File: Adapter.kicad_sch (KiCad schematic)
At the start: 0 parts

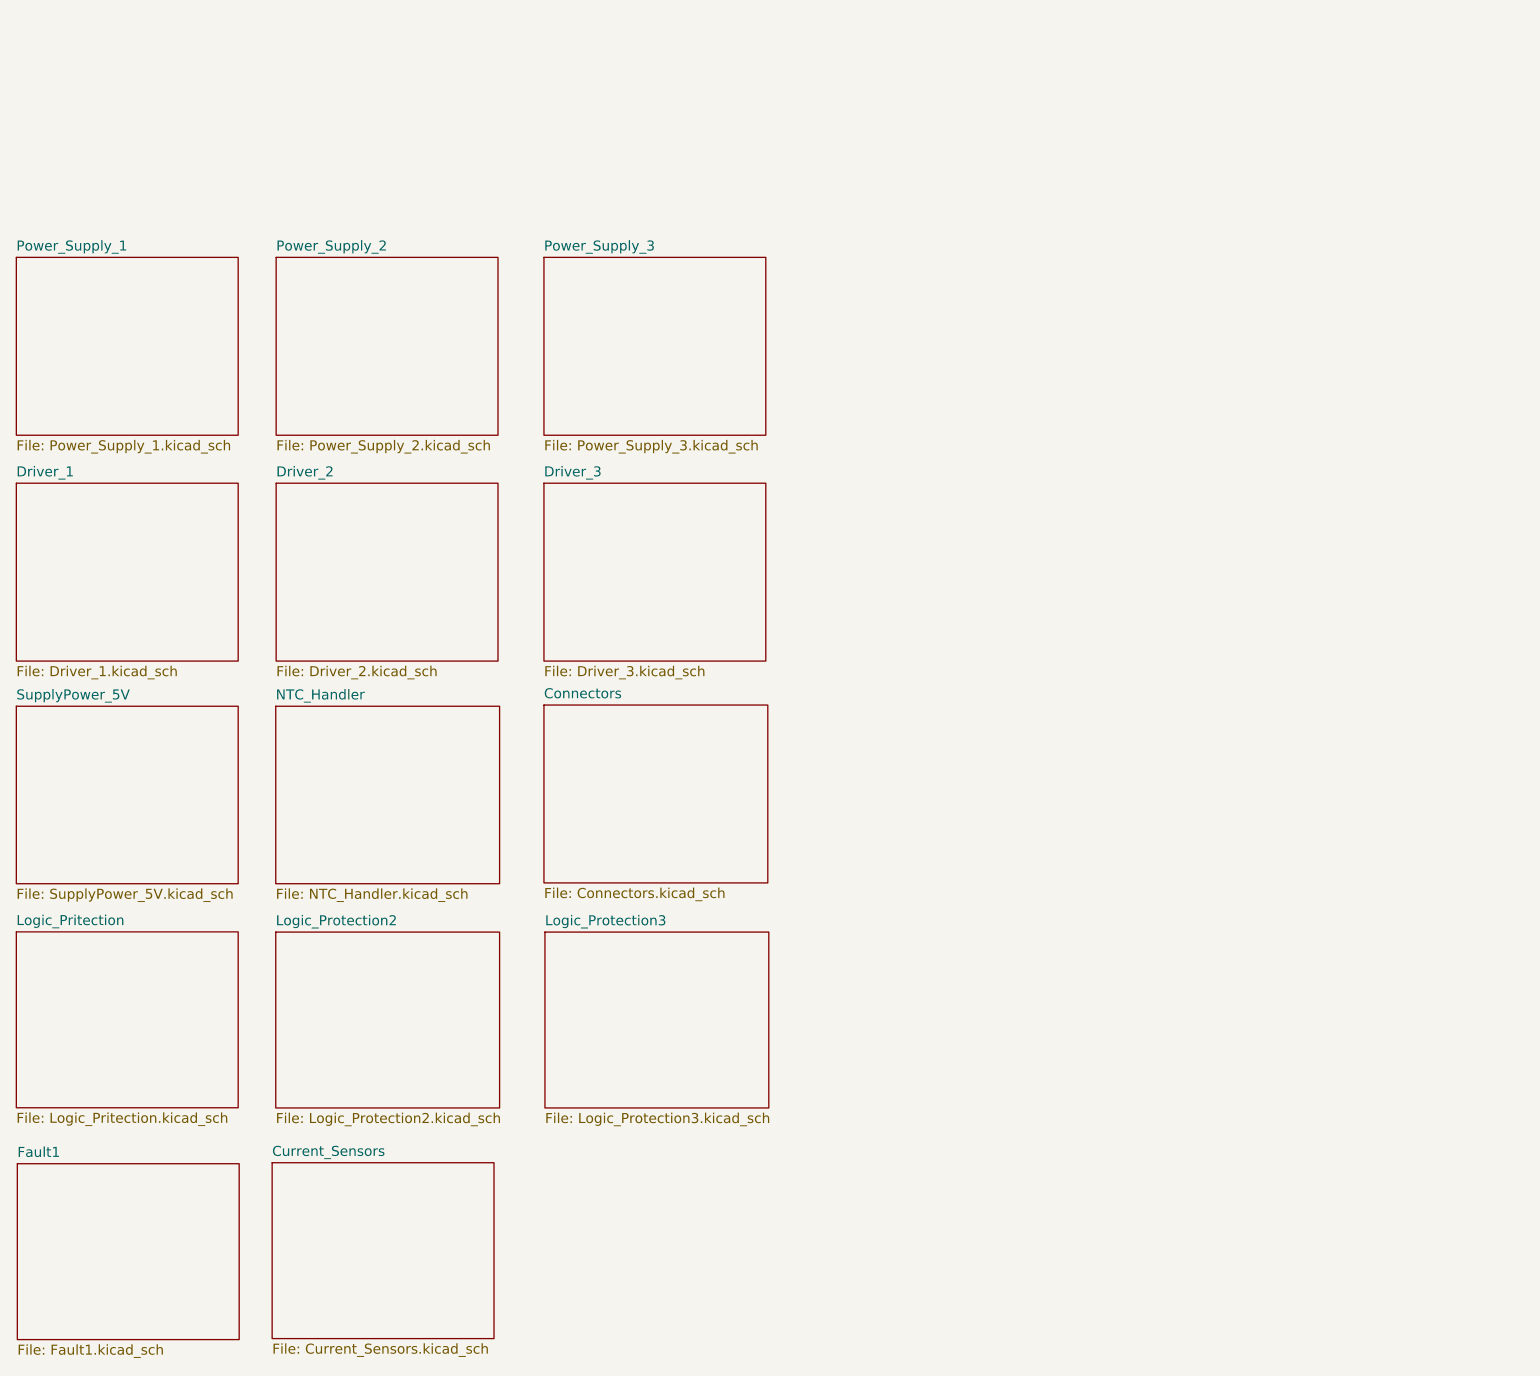
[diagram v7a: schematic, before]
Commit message: VER2.2: добавил фильтры на вход ШИМа и обновил все доки
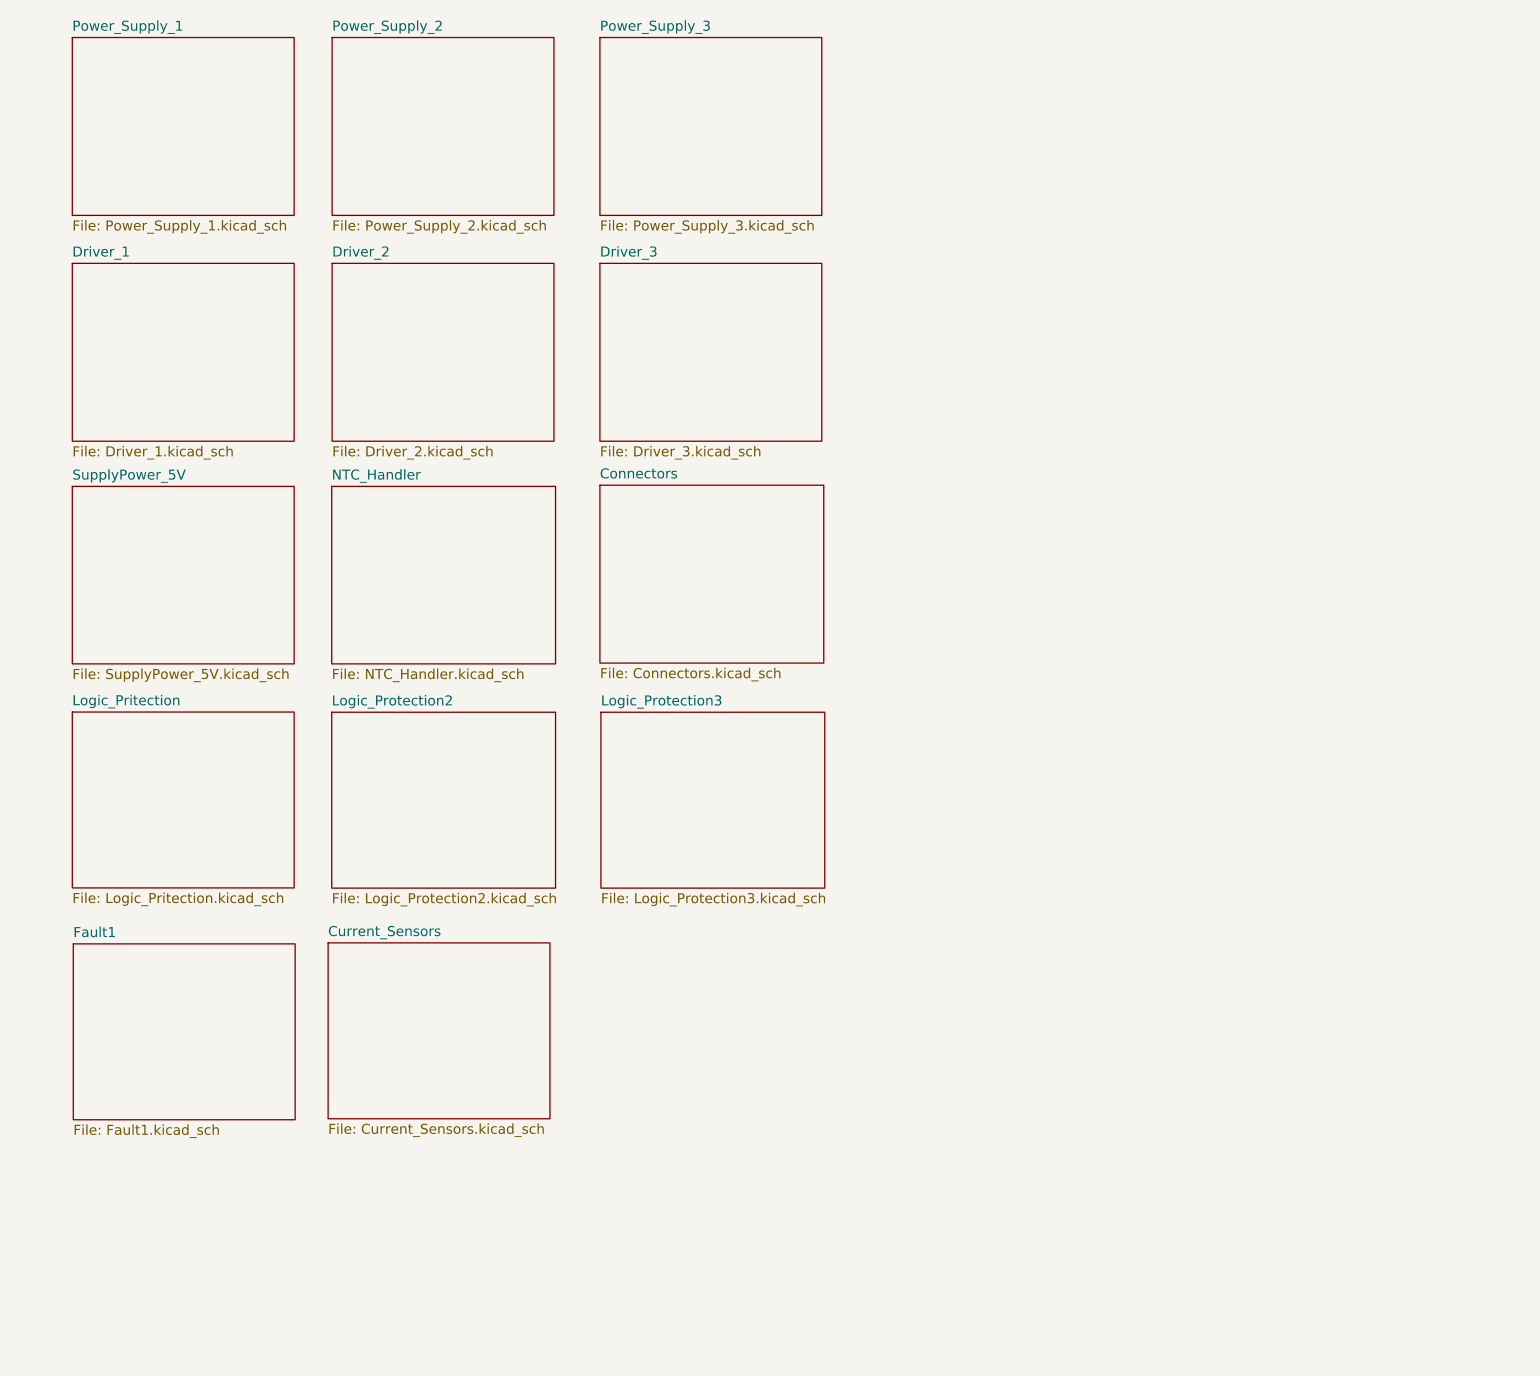
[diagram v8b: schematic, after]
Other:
- company: (none) -> ООО "ЭТТ"
- title: (none) -> Трехфазные драйвера
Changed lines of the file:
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@@
 	(generator "eeschema")
 	(generator_version "9.0")
-	(paper "A4")
-	(sheet
-		(at 18.288 81.28)
+	(paper "A3")
+	(title_block
+		(title "Трехфазные драйвера")
+		(date "2025-06-04")
+		(company "ООО \"ЭТТ\"")
+		(comment 2 "Филатов А.С.")
+		(comment 3 "Сизякин А.В.")
+	)
+	(sheet
+		(at 25.4 53.34)
 		(size 28.194 22.606)
 		(exclude_from_sim no)
@@
 		)
 		(property "Sheetname" "Driver_1"
-			(at 18.288 80.5684 0)
+			(at 25.4 52.6284 0)
 			(effects
 				(font
@@
 		)
 		(property "Sheetfile" "Driver_1.kicad_sch"
-			(at 18.288 104.4706 0)
+			(at 25.4 76.5306 0)
 			(effects
 				(font
@@
 	)
 	(sheet
-		(at 85.344 52.578)
+		(at 92.456 24.638)
 		(size 28.194 22.606)
 		(exclude_from_sim no)
@@
 		)
 		(property "Sheetname" "Power_Supply_3"
-			(at 85.344 51.8664 0)
+			(at 92.456 23.9264 0)
 			(effects
 				(font
@@
 		)
 		(property "Sheetfile" "Power_Supply_3.kicad_sch"
-			(at 85.344 75.7686 0)
+			(at 92.456 47.8286 0)
 			(effects
 				(font
@@
 	)
 	(sheet
-		(at 18.288 109.6264)
+		(at 25.4 81.6864)
 		(size 28.194 22.5552)
 		(exclude_from_sim no)
@@
 		)
 		(property "Sheetname" "SupplyPower_5V"
-			(at 18.288 108.9148 0)
+			(at 25.4 80.9748 0)
 			(effects
 				(font
@@
 		)
 		(property "Sheetfile" "SupplyPower_5V.kicad_sch"
-			(at 18.288 132.7662 0)
+			(at 25.4 104.8262 0)
 			(effects
 				(font
@@
 	)
 	(sheet
-		(at 85.344 81.28)
+		(at 92.456 53.34)
 		(size 28.194 22.606)
 		(exclude_from_sim no)
@@
 		)
 		(property "Sheetname" "Driver_3"
-			(at 85.344 80.5684 0)
+			(at 92.456 52.6284 0)
 			(effects
 				(font
@@
 		)
 		(property "Sheetfile" "Driver_3.kicad_sch"
-			(at 85.344 104.4706 0)
+			(at 92.456 76.5306 0)
 			(effects
 				(font
@@
 	)
 	(sheet
-		(at 50.8 167.64)
+		(at 57.912 139.7)
 		(size 28.194 22.352)
 		(exclude_from_sim no)
@@
 		)
 		(property "Sheetname" "Current_Sensors"
-			(at 50.8 166.9284 0)
+			(at 57.912 138.9884 0)
 			(effects
 				(font
@@
 		)
 		(property "Sheetfile" "Current_Sensors.kicad_sch"
-			(at 50.8 190.5766 0)
+			(at 57.912 162.6366 0)
 			(effects
 				(font
@@
 	)
 	(sheet
-		(at 51.308 81.28)
+		(at 58.42 53.34)
 		(size 28.194 22.606)
 		(exclude_from_sim no)
@@
 		)
 		(property "Sheetname" "Driver_2"
-			(at 51.308 80.5684 0)
+			(at 58.42 52.6284 0)
 			(effects
 				(font
@@
 		)
 		(property "Sheetfile" "Driver_2.kicad_sch"
-			(at 51.308 104.4706 0)
+			(at 58.42 76.5306 0)
 			(effects
 				(font
@@
 	)
 	(sheet
-		(at 18.288 138.303)
+		(at 25.4 110.363)
 		(size 28.194 22.352)
 		(exclude_from_sim no)
@@
 		)
 		(property "Sheetname" "Logic_Pritection"
-			(at 18.288 137.5914 0)
+			(at 25.4 109.6514 0)
 			(effects
 				(font
@@
 		)
 		(property "Sheetfile" "Logic_Pritection.kicad_sch"
-			(at 18.288 161.2396 0)
+			(at 25.4 133.2996 0)
 			(effects
 				(font
@@
 	)
 	(sheet
-		(at 18.288 52.578)
+		(at 25.4 24.638)
 		(size 28.194 22.606)
 		(exclude_from_sim no)
@@
 		)
 		(property "Sheetname" "Power_Supply_1"
-			(at 18.288 51.8664 0)
+			(at 25.4 23.9264 0)
 			(effects
 				(font
@@
 		)
 		(property "Sheetfile" "Power_Supply_1.kicad_sch"
-			(at 18.288 75.7686 0)
+			(at 25.4 47.8286 0)
 			(effects
 				(font
@@
 	)
 	(sheet
-		(at 85.344 109.474)
+		(at 92.456 81.534)
 		(size 28.448 22.606)
 		(exclude_from_sim no)
@@
 		)
 		(property "Sheetname" "Connectors"
-			(at 85.344 108.7624 0)
+			(at 92.456 80.8224 0)
 			(effects
 				(font
@@
 		)
 		(property "Sheetfile" "Connectors.kicad_sch"
-			(at 85.344 132.6646 0)
+			(at 92.456 104.7246 0)
 			(effects
 				(font
@@
 	)
 	(sheet
-		(at 51.2572 109.6264)
+		(at 58.3692 81.6864)
 		(size 28.448 22.5552)
 		(exclude_from_sim no)
@@
 		)
 		(property "Sheetname" "NTC_Handler"
-			(at 51.2572 108.9148 0)
+			(at 58.3692 80.9748 0)
 			(effects
 				(font
@@
 		)
 		(property "Sheetfile" "NTC_Handler.kicad_sch"
-			(at 51.2572 132.7662 0)
+			(at 58.3692 104.8262 0)
 			(effects
 				(font
@@
 	)
 	(sheet
-		(at 18.415 167.767)
+		(at 25.527 139.827)
 		(size 28.194 22.352)
 		(exclude_from_sim no)
@@
 		)
 		(property "Sheetname" "Fault1"
-			(at 18.415 167.0554 0)
+			(at 25.527 139.1154 0)
 			(effects
 				(font
@@
 		)
 		(property "Sheetfile" "Fault1.kicad_sch"
-			(at 18.415 190.7036 0)
+			(at 25.527 162.7636 0)
 			(effects
 				(font
@@
 	)
 	(sheet
-		(at 51.2572 138.3284)
+		(at 58.3692 110.3884)
 		(size 28.448 22.352)
 		(exclude_from_sim no)
@@
 		)
 		(property "Sheetname" "Logic_Protection2"
-			(at 51.2572 137.6168 0)
+			(at 58.3692 109.6768 0)
 			(effects
 				(font
@@
 		)
 		(property "Sheetfile" "Logic_Protection2.kicad_sch"
-			(at 51.2572 161.265 0)
+			(at 58.3692 133.325 0)
 			(effects
 				(font
@@
 	)
 	(sheet
-		(at 51.308 52.578)
+		(at 58.42 24.638)
 		(size 28.194 22.606)
 		(exclude_from_sim no)
@@
 		)
 		(property "Sheetname" "Power_Supply_2"
-			(at 51.308 51.8664 0)
+			(at 58.42 23.9264 0)
 			(effects
 				(font
@@
 		)
 		(property "Sheetfile" "Power_Supply_2.kicad_sch"
-			(at 51.308 75.7686 0)
+			(at 58.42 47.8286 0)
 			(effects
 				(font
@@
 	)
 	(sheet
-		(at 85.471 138.3284)
+		(at 92.583 110.3884)
 		(size 28.448 22.352)
 		(exclude_from_sim no)
@@
 		)
 		(property "Sheetname" "Logic_Protection3"
-			(at 85.471 137.6168 0)
+			(at 92.583 109.6768 0)
 			(effects
 				(font
@@
 		)
 		(property "Sheetfile" "Logic_Protection3.kicad_sch"
-			(at 85.471 161.265 0)
+			(at 92.583 133.325 0)
 			(effects
 				(font
@@
 	)
 	(embedded_fonts no)
+	(embedded_files
+		(file
+			(name "gost_landscape.kicad_wks")
+			(type worksheet)
+			(data |KLUv/WC6IO0nAEYqgjFAc9pUwaAq7rGQvf7J+ej28lrFVi+Ra0Qr0XvBpp0PVIKJocju3inLuMxu
+				WJMBZ+8LfABnAHoALNo2GUZx9Wyv+vGO7GqGEQi0h1NBVbQbu4asUlxtNdu0DUOHHXuz3S4LorjC
+				2E01EGgMV8+VUWw3dfNo1moMH81SFXzgYBtVTc4wznZ5FqxD7VTQq7ccP9gGTKJmWIeqoOVcJzCQ
+				DVVL8SfCVhDFDBBgIzTR1VmonOtDBRi2oWoZrJTd7jX9n7Khe3Oye/9Ms1rmYPfHZufeRc3LSf+n
+				jA0dvmaRc3bwZWv+XePfzun8KCGM/7Cfewzne/kzOnz97xpCdtQnfM1OdoRSwyL6ns9/yCEXdTKt
+				OdMw+9FeW47UoQcp1/Kgs+ReeFeQbod89jhy6K+b4b9sl8309ehUweEadu1UTChOpuuy4U1LLpJO
+				lVtSuhJakbPaCV0eintGDej97uhEuhmOcrWX1TbJb5lclmu6pItyMa5v1WZ1wyIHzIIiICx/hlaE
+				zSDtgyDQGGvlWpxSbsstXdJLQQAB1cP21+/uObTaZWza0c22HZYs36ROMpS0m+FjF6MbeD2fZOgw
+				wZ3rg/x/m2kOFM+HkHnw/SDTPLsg89wrZHil5ZLQ0Wmkp4vQlk4KkREFxB1+PPn90ttfe+myyeUD
+				umO5J3flmlwuU5xO7sejFKfRiSWBbahBUahmpCAFSSHDGnGRwBiC1Z0dskgQgjAUw4AcCGIcAhlC
+				HCFEQAwhhBhjREauHS1W9GqoT2ej9oib6AkUZ1xytemsseM0xpmg8F4VpZ0BeQEinRqXR/LHvcXM
+				zxBtuIUaw8HcSNawPE002iKV23H6UV273ntSIAlTA5N1ZdrndCiVe6uBaRiHYYiKq9GgNrTeNTRf
+				NfUJ/32bWh9/57DHw7uQxz4ULHfFeApmWDLvyo3GHRcRbczSKYx08fXGVh6xzSXRvDpB6BApYY8y
+				6sEbrKBGeegRkrjMrCrrLxeLYxp0HswTCskvDBMXTHE/T+ByeqaPP3qdKzND8/1VD3bUDeJn0Y9z
+				gDZPfEvFjAaAJZpbLUtz3kaxhDe3Snk/4OyFwqFNmJyv7iYuCzQrtB3ykyQKiwBJcw2JxNU32g3/
+				kVAxeFgRdQg12uIi1pyRGPpIH4Xa+rlwJouAD+8zrEHs/Mj95yRfSbzxr/d0A4lRg1eZtAqJQBlT
+				3zHGdrqzkPo5zEAHci6R5WaJ7M8aOMeYTH8ylU/JOjqDbeYB3A/SED8iC0uFsZZlGFxjlGVAmFBW
+				Sg295mriH68MGT6sxAPRzPNjscyiXi6CHelA4On6CGhR0TBQg6X1agUnjA2o+EQ8+EMjOt0EE3O1
+				KZXjk96NgCgPyIEYPya3WbCT53yDvYomiSBeq3cTdXyh8ErjMLtLd9lDpdvsZ53W2mh1ArZ1o9W/
+				pn4MvGAJn4RflojuA5iT3WAhYm7x+ywpKbA6SP8AsvhaPKoyXAVabGD5KqtYRIZHh+1qjSosK7Zk
+				WnUXr26KKLGZ9FmofbXdLWEkLIYWnz6CoHAJ1aETYyMLDNADH7/BUkuXmDcZVyKv/jweRknOlknx
+				InFQ+uGQOpYGNF5vgyfg9IZKup03LTR7DEu7ADGKQmGCR30jTPWNMAURYVmFlx3OQiIuT/p0NIV4
+				k5jbGQYYpblIqpu8oZ6A0nlGAufJ/aGmRk8NeaaILFcB|
+			)
+			(checksum "9180C2D8C133E7F089AA5E43F4962E04")
+		)
+	)
 )
